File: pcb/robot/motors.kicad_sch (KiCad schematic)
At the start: 27 parts, among them J3 Conn_01x06_MountingPin, J5 Conn_01x06_MountingPin, J6 MotorCable, J7 MotorCable, Q6 SN74AHC125RGYR, U8 DRV8830DRCR, U9 DRV8830DRCR

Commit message: Re-unify USB-PD module into main board (single-PCB architecture) (#17)
Merges the USB-PD module circuitry back into the main robot board as
a single PCB, reversing the earlier main-board/USB-PD-daughter-board
split. Full re-route and re-placement of the combined design:

- Consolidated low-profile parts toward the board center, using the
  space freed up by relocated capacitors, for better overall use of
  the available area.
- Kept all 0-ohm test/isolation jumpers in accessible locations for
  bench testing.
- Added/corrected footprints for several parts that had broken or
  incorrect footprints (DDC6_TEX variants, SOT-23-6, SOT-23-3,
  R0402).

Carries forward every closed correction issue and update made since
the original split: #3 (CC jumpers), #6 (IC1.ON pull-down), #14/#15
(ADC divider, motor connector pinout), #16, #18 (I2C isolation
jumpers), #19 (charger-sense GPIO interrupt), plus the BOM/pricing
updates, LED changes, and MAX77642 replacement.

Verified via kicad-cli ERC/DRC + netlist diff against the pre-merge
board: 0 unconnected items (unchanged), no new DRC error-level
violations besides one pre-existing excluded item, and the #6
(IC1.ON pull-down) and #19 (charger-sense GPIO interrupt) circuits
confirmed intact at the net-topology level despite the full-board
re-annotation changing most reference designators. Most of the raw
diff size is a KiCad 9 footprint-format upgrade (pre-2023 format
rewritten to current) rather than design changes - spot-checked
against unrelated footprints (e.g. mounting holes), which show
identical geometry under the new syntax.
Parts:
- NT20: renamed from NT17; symbol Device:NetTie_2 -> robot:NetTie_2
- R100: renamed from R39; symbol Device:R -> robot:R
- R97: renamed from R36; symbol Device:R -> robot:R
- R98: renamed from R37; symbol Device:R -> robot:R
- R99: renamed from R38; symbol Device:R -> robot:R
- renumbered C44 to C119, C40 to C82, C41 to C83, C42 to C86, C43 to C87, J6 to J5, J5 to J6, J3 to J7, J7 to J8, R31 to R102, R26 to R90, R27 to R91, R28 to R93, R29 to R94, R30 to R95, U8 to U25, U9 to U26
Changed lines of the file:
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@@
 	)
 	(symbol
-		(lib_id "Device:NetTie_2")
+		(lib_id "robot:NetTie_2")
 		(at 67.31 129.54 0)
 		(mirror y)
@@
 		(on_board yes)
 		(dnp no)
-		(property "Reference" "NT17"
+		(property "Reference" "NT20"
 			(at 67.818 132.334 0)
 			(effects
@@
 			(project "robot"
 				(path "/0c7b298e-2d07-4b1f-b033-e95f02d45089/4bf796fd-fdb4-45d1-808a-a634d5f4571e"
-					(reference "NT17")
+					(reference "NT20")
 					(unit 1)
 				)
@@
 		(dnp no)
 		(fields_autoplaced yes)
-		(property "Reference" "J3"
+		(property "Reference" "J7"
 			(at 242.57 52.4256 0)
 			(effects
@@
 			(project "robot"
 				(path "/0c7b298e-2d07-4b1f-b033-e95f02d45089/4bf796fd-fdb4-45d1-808a-a634d5f4571e"
-					(reference "J3")
+					(reference "J7")
 					(unit 1)
 				)
@@
 		(dnp yes)
 		(fields_autoplaced yes)
-		(property "Reference" "R27"
+		(property "Reference" "R91"
 			(at 62.23 139.6999 0)
 			(effects
@@
 			(project "robot"
 				(path "/0c7b298e-2d07-4b1f-b033-e95f02d45089/4bf796fd-fdb4-45d1-808a-a634d5f4571e"
-					(reference "R27")
+					(reference "R91")
 					(unit 1)
 				)
@@
 		(dnp no)
 		(fields_autoplaced yes)
-		(property "Reference" "J5"
+		(property "Reference" "J6"
 			(at 234.95 52.4256 0)
 			(effects
@@
 			(project "robot"
 				(path "/0c7b298e-2d07-4b1f-b033-e95f02d45089/4bf796fd-fdb4-45d1-808a-a634d5f4571e"
-					(reference "J5")
+					(reference "J6")
 					(unit 1)
 				)
@@
 		(on_board yes)
 		(dnp no)
-		(property "Reference" "C42"
+		(property "Reference" "C86"
 			(at 134.62 48.2599 0)
 			(effects
@@
 			(project "robot"
 				(path "/0c7b298e-2d07-4b1f-b033-e95f02d45089/4bf796fd-fdb4-45d1-808a-a634d5f4571e"
-					(reference "C42")
+					(reference "C86")
 					(unit 1)
 				)
@@
 		(dnp no)
 		(fields_autoplaced yes)
-		(property "Reference" "R28"
+		(property "Reference" "R93"
 			(at 69.85 40.6399 0)
 			(effects
@@
 			(project "robot"
 				(path "/0c7b298e-2d07-4b1f-b033-e95f02d45089/4bf796fd-fdb4-45d1-808a-a634d5f4571e"
-					(reference "R28")
+					(reference "R93")
 					(unit 1)
 				)
@@
 		(on_board yes)
 		(dnp no)
-		(property "Reference" "C40"
+		(property "Reference" "C82"
 			(at 121.92 48.2599 0)
 			(effects
@@
 			(project "robot"
 				(path "/0c7b298e-2d07-4b1f-b033-e95f02d45089/4bf796fd-fdb4-45d1-808a-a634d5f4571e"
-					(reference "C40")
+					(reference "C82")
 					(unit 1)
 				)
@@
 		(dnp yes)
 		(fields_autoplaced yes)
-		(property "Reference" "R26"
+		(property "Reference" "R90"
 			(at 62.23 68.5799 0)
 			(effects
@@
 			(project "robot"
 				(path "/0c7b298e-2d07-4b1f-b033-e95f02d45089/4bf796fd-fdb4-45d1-808a-a634d5f4571e"
-					(reference "R26")
+					(reference "R90")
 					(unit 1)
 				)
@@
 		(dnp yes)
 		(fields_autoplaced yes)
-		(property "Reference" "J7"
+		(property "Reference" "J8"
 			(at 254 66.675 0)
 			(effects
@@
 			(project "robot"
 				(path "/0c7b298e-2d07-4b1f-b033-e95f02d45089/4bf796fd-fdb4-45d1-808a-a634d5f4571e"
-					(reference "J7")
+					(reference "J8")
 					(unit 1)
 				)
@@
 		(dnp no)
 		(fields_autoplaced yes)
-		(property "Reference" "R31"
+		(property "Reference" "R102"
 			(at 76.2 110.4899 0)
 			(effects
@@
 			(project "robot"
 				(path "/0c7b298e-2d07-4b1f-b033-e95f02d45089/4bf796fd-fdb4-45d1-808a-a634d5f4571e"
-					(reference "R31")
+					(reference "R102")
 					(unit 1)
 				)
@@
 	)
 	(symbol
-		(lib_id "Device:R")
+		(lib_id "robot:R")
 		(at 72.39 121.92 90)
 		(unit 1)
@@
 		(on_board yes)
 		(dnp no)
-		(property "Reference" "R38"
+		(property "Reference" "R99"
 			(at 75.692 120.396 90)
 			(effects
@@
 			(project "robot"
 				(path "/0c7b298e-2d07-4b1f-b033-e95f02d45089/4bf796fd-fdb4-45d1-808a-a634d5f4571e"
-					(reference "R38")
+					(reference "R99")
 					(unit 1)
 				)
@@
 	)
 	(symbol
-		(lib_id "Device:R")
+		(lib_id "robot:R")
 		(at 72.39 124.46 90)
 		(unit 1)
@@
 		(on_board yes)
 		(dnp no)
-		(property "Reference" "R39"
+		(property "Reference" "R100"
 			(at 73.66 126.492 90)
 			(effects
@@
 			(project "robot"
 				(path "/0c7b298e-2d07-4b1f-b033-e95f02d45089/4bf796fd-fdb4-45d1-808a-a634d5f4571e"
-					(reference "R39")
+					(reference "R100")
 					(unit 1)
 				)
@@
 		(dnp no)
 		(fields_autoplaced yes)
-		(property "Reference" "R30"
+		(property "Reference" "R95"
 			(at 70.358 140.1353 0)
 			(effects
@@
 			(project "robot"
 				(path "/0c7b298e-2d07-4b1f-b033-e95f02d45089/4bf796fd-fdb4-45d1-808a-a634d5f4571e"
-					(reference "R30")
+					(reference "R95")
 					(unit 1)
 				)
@@
 	)
 	(symbol
-		(lib_id "Device:R")
+		(lib_id "robot:R")
 		(at 71.12 50.8 90)
 		(unit 1)
@@
 		(on_board yes)
 		(dnp no)
-		(property "Reference" "R36"
+		(property "Reference" "R97"
 			(at 71.12 48.26 90)
 			(effects
@@
 			(project "robot"
 				(path "/0c7b298e-2d07-4b1f-b033-e95f02d45089/4bf796fd-fdb4-45d1-808a-a634d5f4571e"
-					(reference "R36")
+					(reference "R97")
 					(unit 1)
 				)
@@
 		(on_board yes)
 		(dnp no)
-		(property "Reference" "C43"
+		(property "Reference" "C87"
 			(at 134.62 119.3799 0)
 			(effects
@@
 			(project "robot"
 				(path "/0c7b298e-2d07-4b1f-b033-e95f02d45089/4bf796fd-fdb4-45d1-808a-a634d5f4571e"
-					(reference "C43")
+					(reference "C87")
 					(unit 1)
 				)
@@
 		(dnp yes)
 		(fields_autoplaced yes)
-		(property "Reference" "J6"
+		(property "Reference" "J5"
 			(at 217.17 66.675 0)
 			(effects
@@
 			(project "robot"
 				(path "/0c7b298e-2d07-4b1f-b033-e95f02d45089/4bf796fd-fdb4-45d1-808a-a634d5f4571e"
-					(reference "J6")
+					(reference "J5")
 					(unit 1)
 				)
@@
 		(dnp no)
 		(fields_autoplaced yes)
-		(property "Reference" "U9"
+		(property "Reference" "U26"
 			(at 96.52 109.22 0)
 			(effects
@@
 			(project "robot"
 				(path "/0c7b298e-2d07-4b1f-b033-e95f02d45089/4bf796fd-fdb4-45d1-808a-a634d5f4571e"
-					(reference "U9")
+					(reference "U26")
 					(unit 1)
 				)
@@
 		(on_board yes)
 		(dnp no)
-		(property "Reference" "C41"
+		(property "Reference" "C83"
 			(at 121.92 119.3799 0)
 			(effects
@@
 			(project "robot"
 				(path "/0c7b298e-2d07-4b1f-b033-e95f02d45089/4bf796fd-fdb4-45d1-808a-a634d5f4571e"
-					(reference "C41")
+					(reference "C83")
 					(unit 1)
 				)
@@
 		(dnp no)
 		(fields_autoplaced yes)
-		(property "Reference" "U8"
+		(property "Reference" "U25"
 			(at 96.52 38.1 0)
 			(effects
@@
 			(project "robot"
 				(path "/0c7b298e-2d07-4b1f-b033-e95f02d45089/4bf796fd-fdb4-45d1-808a-a634d5f4571e"
-					(reference "U8")
+					(reference "U25")
 					(unit 1)
 				)
@@
 	)
 	(symbol
-		(lib_id "Device:R")
+		(lib_id "robot:R")
 		(at 71.12 53.34 90)
 		(unit 1)
@@
 		(on_board yes)
 		(dnp no)
-		(property "Reference" "R37"
+		(property "Reference" "R98"
 			(at 70.866 55.626 90)
 			(effects
@@
 			(project "robot"
 				(path "/0c7b298e-2d07-4b1f-b033-e95f02d45089/4bf796fd-fdb4-45d1-808a-a634d5f4571e"
-					(reference "R37")
+					(reference "R98")
 					(unit 1)
 				)
@@
 		(on_board yes)
 		(dnp no)
-		(property "Reference" "C44"
+		(property "Reference" "C119"
 			(at 255.27 160.0199 0)
 			(effects
@@
 			(project "robot"
 				(path "/0c7b298e-2d07-4b1f-b033-e95f02d45089/4bf796fd-fdb4-45d1-808a-a634d5f4571e"
-					(reference "C44")
+					(reference "C119")
 					(unit 1)
 				)
@@
 		(dnp no)
 		(fields_autoplaced yes)
-		(property "Reference" "R29"
+		(property "Reference" "R94"
 			(at 70.358 69.0153 0)
 			(effects
@@
 			(project "robot"
 				(path "/0c7b298e-2d07-4b1f-b033-e95f02d45089/4bf796fd-fdb4-45d1-808a-a634d5f4571e"
-					(reference "R29")
+					(reference "R94")
 					(unit 1)
 				)

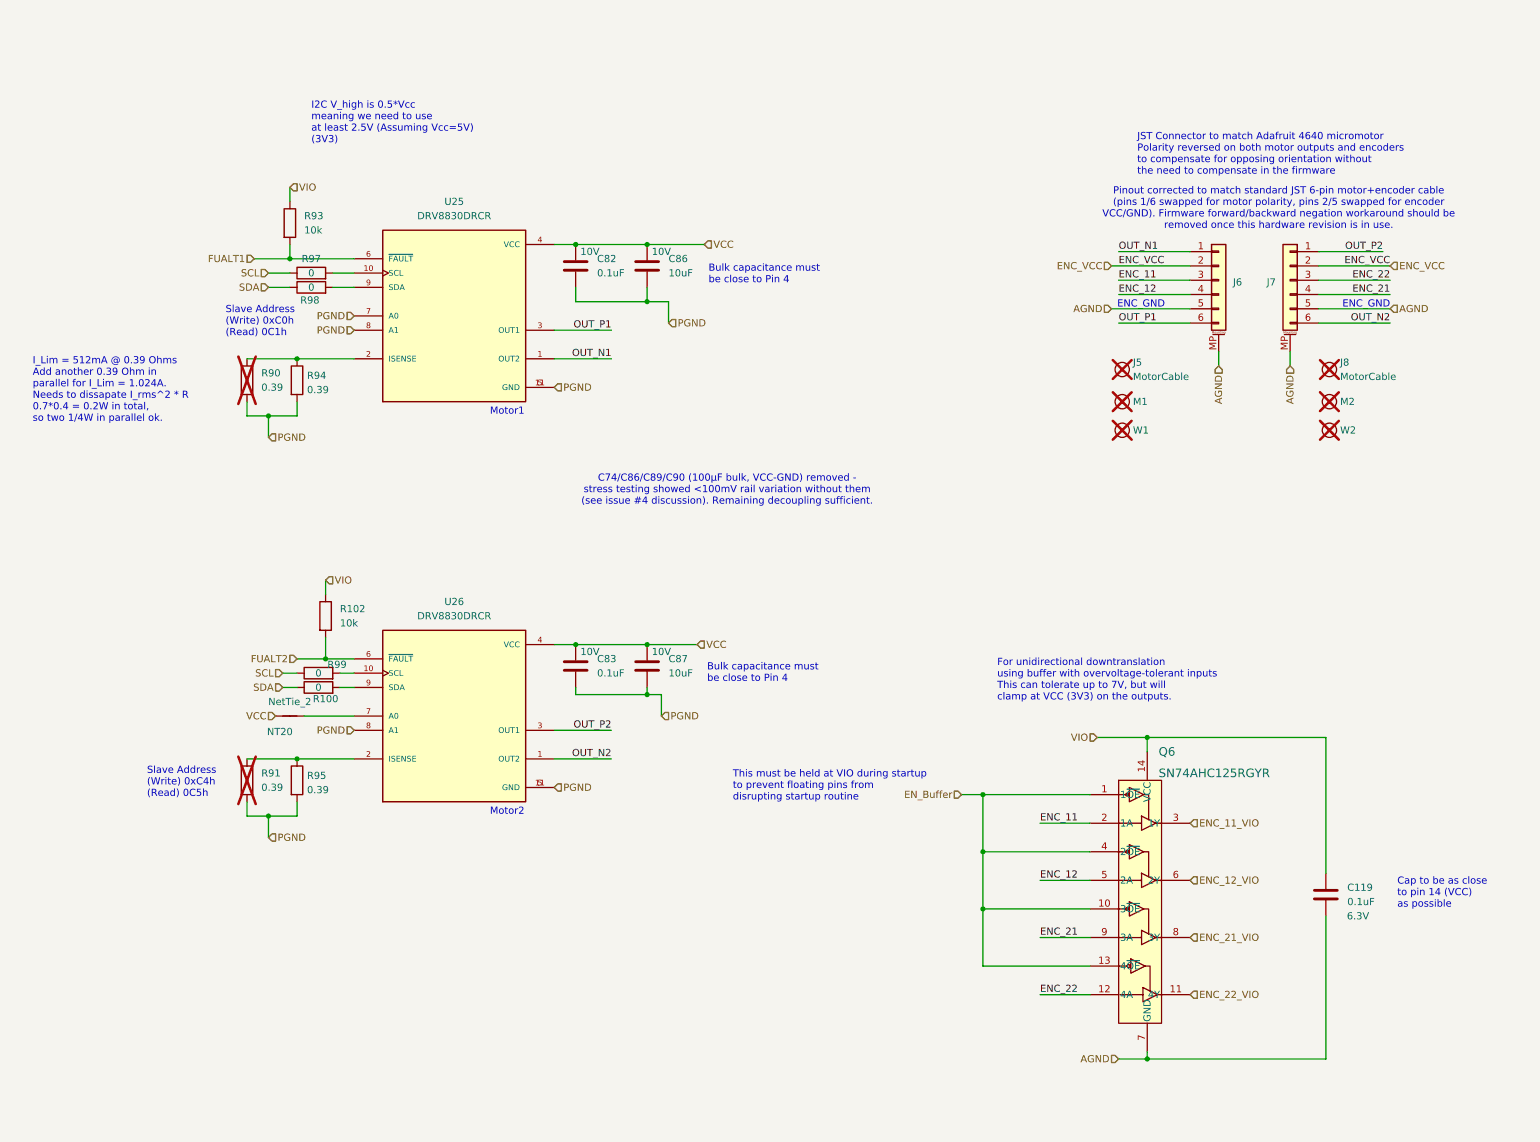
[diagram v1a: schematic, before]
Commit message: Add active shunt clamp and restore bulk-cap footprints for motor VCC (#22)
Comparator-based shunt (U32/U33/Q7/R124) clamps /MOTORS/VCC around
5.6V/5.4V hysteresis, dumping regen energy through R124 to PGND.
Three more 2.7ohm positions (R125-127) left DNP for thermal tuning
after bench testing.

Also restores C132-135 (100uF, DNP) bulk-cap footprints on the same
rail, removed in #16 - footprint only, final value still pending
Christopher's testing.

Verified with kicad-cli: ERC clean, DRC shows zero schematic/PCB
parity mismatches and zero unconnected items.
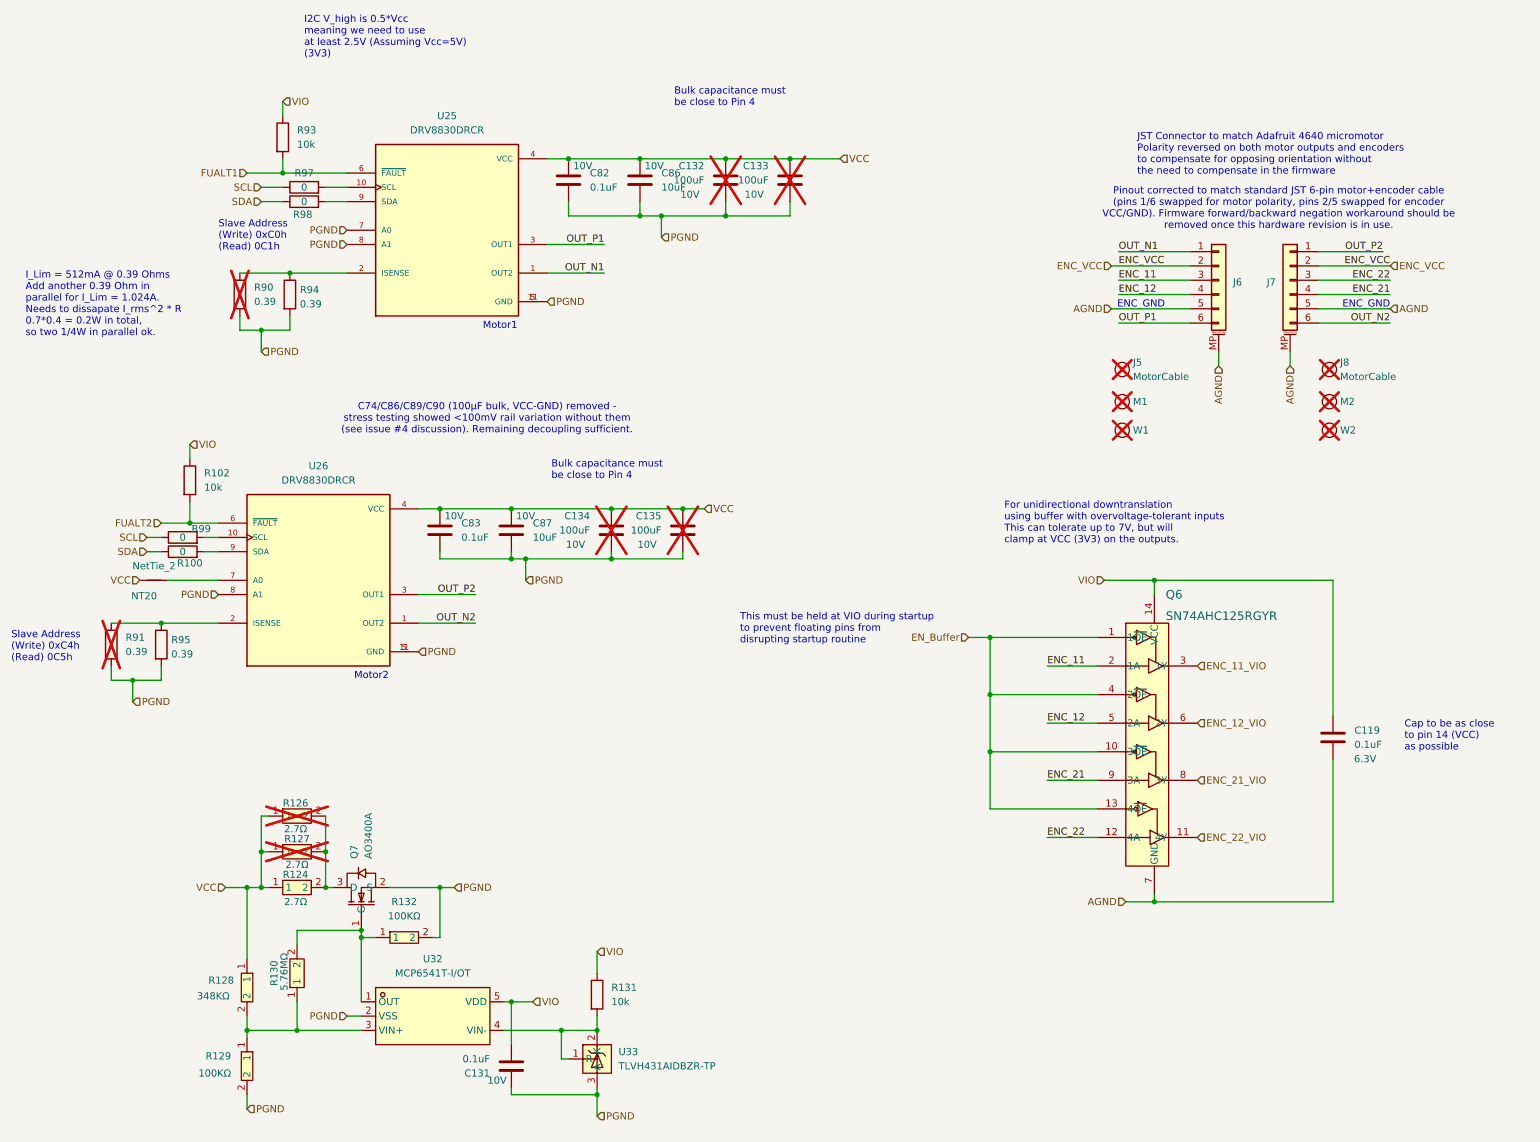
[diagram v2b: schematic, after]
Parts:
- added C131: 0.1uF, robot:C_0402_1005Metric, symbol robot:C
- added C132, C133, C134, C135: 100uF, robot:CP_Elec_APXJ100ARA271MF61G, symbol robot:C
- added Q7: AO3400A, easyeda2kicad:SOT-23-3_L2.9-W1.3-P1.90-LS2.4-BR, symbol easyeda2kicad:AO3400A
- added R124, R126, R127: 2.7Ω, easyeda2kicad:R2512, symbol easyeda2kicad:FRC2512F2R70TS
- added R128: 348KΩ, easyeda2kicad:R0603, symbol easyeda2kicad:0603WAF3483T5E
- added R129, R132: 100KΩ, easyeda2kicad:R0603, symbol easyeda2kicad:0603WAF1003T5E
- added R130: 5.76MΩ, easyeda2kicad:R0603, symbol easyeda2kicad:0603WAF5904T5E
- added R131: 10k, robot:R_0603_1608Metric, symbol robot:R
- added U32: MCP6541T-I/OT, easyeda2kicad:SOT-23-5_L3.0-W1.7-P0.95-LS2.8-BR, symbol easyeda2kicad:MCP6541T-I_OT
- added U33: TLVH431AIDBZR-TP, easyeda2kicad:SOT-23-3_L3.0-W1.6-P1.90-LS2.8-BR, symbol easyeda2kicad:TLVH431AIDBZR-TP
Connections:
- net PGND: now also C131.1, C132.2, C133.2, C134.2, C135.2, Q7.2 (S), R129.2, R132.2, U32.2 (VSS), U33.3 (A)
- net VCC: now also C132.1, C133.1, C134.1, C135.1, R124.1, R126.1, R127.1, R128.1
- net VIO: now also C131.2, R131.1, U32.5 (VDD)
- new net: Q7.3 (D), R124.2, R126.2, R127.2
- new net: R128.2, R129.1, R130.1, U32.3 (VIN+)
- new net: Q7.1 (G), R130.2, R132.1, U32.1 (OUT)
- new net: R131.2, U32.4 (VIN-), U33.1 (R), U33.2 (K)
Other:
- moved on the sheet: C119, C82, C83, C86, C87, NT20, Q6, R100, R102, R90, R91, R93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

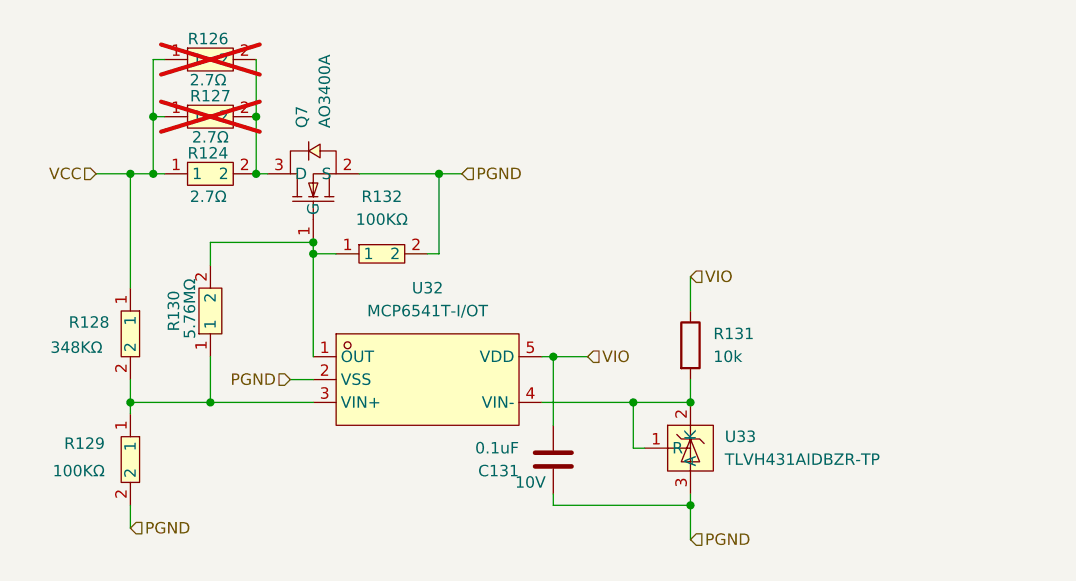
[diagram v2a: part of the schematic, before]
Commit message: Add switch-open discharge detector and low-power OV reference (#22, #23)
U34 (new, MCP6541 on IC1-VBIAS) senses the power switch via
Net-(IC1-ON) and forces Q7/R124 (#22's shunt) to discharge
/MOTORS/VCC when the switch opens, independent of the 3V3 rail.
OR'd into Q7's gate through D11/D12 alongside U32's existing
overvoltage trip - discharges in ~2.2ms vs. the ~500-600ms the
MAX77857 was timing out at.

Also swaps U33 (TLVH431) for a MAX6006A micropower reference and
bumps R131 to 412k, per Christopher's request on #22 - cuts the
clamp's standing current from ~218uA to ~18uA with the same
5.6V/5.4V thresholds.

Verified with kicad-cli: ERC clean, 0 unconnected items, schematic
parity clean (pre-existing U12 footprint mismatch aside).
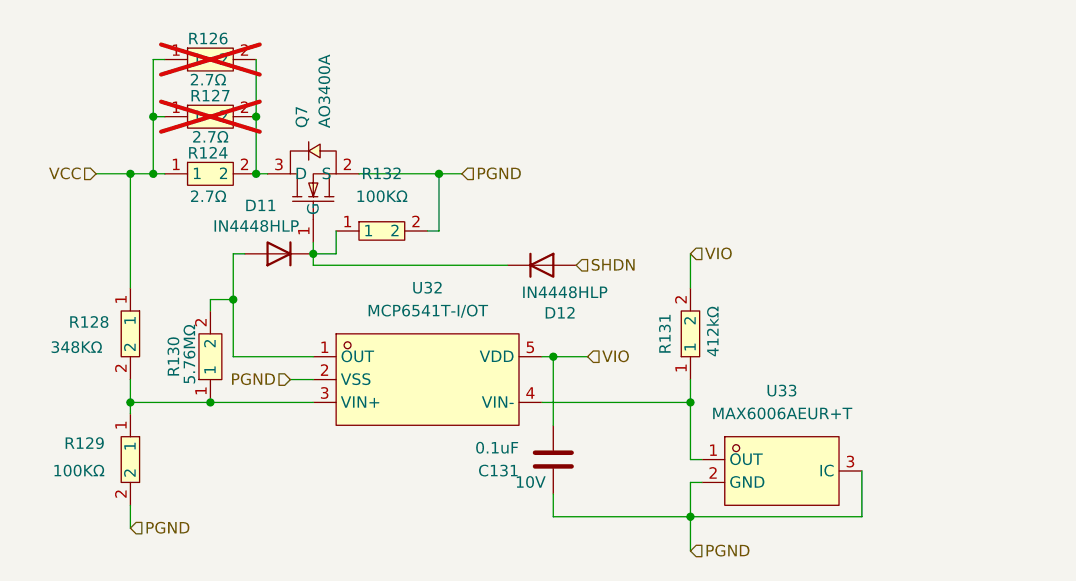
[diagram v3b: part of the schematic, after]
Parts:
- removed R131: 10k, robot:R_0603_1608Metric, symbol robot:R
- removed U33: TLVH431AIDBZR-TP, easyeda2kicad:SOT-23-3_L3.0-W1.6-P1.90-LS2.8-BR, symbol easyeda2kicad:TLVH431AIDBZR-TP
- added D11, D12: IN4448HLP, robot:D_0402_1005Metric, symbol robot:D
- added R131: 412kΩ, easyeda2kicad:R0402, symbol easyeda2kicad:0402WGF4123TCE
- added U33: MAX6006AEUR+T, easyeda2kicad:SOT-23-3_L2.9-W1.3-P0.95-LS2.4-BR, symbol easyeda2kicad:MAX6006AEUR+T
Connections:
- net PGND: now also U33.2 (GND), U33.3 (IC)
- net VIO: now also R131.2
- net at R130.2, U32.1 (OUT): now also D11.2 (A); no longer Q7.1 (G), R132.1
- net at U32.4 (VIN-): now also R131.1, U33.1 (OUT)
- new net: D11.1 (K), D12.1 (K), Q7.1 (G), R132.1
- new net SHDN: D12.2 (A)
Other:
- moved on the sheet: R130, R132
